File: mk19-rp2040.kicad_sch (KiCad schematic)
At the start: 145 parts, among them J1 USB_C_Receptacle_USB2.0, J10 Conn_01x02, J11 Conn_01x03_Socket, J12 USB_C_Receptacle_USB2.0, J13 USB_C_Receptacle_USB2.0, J2 Conn_01x03_Socket, J3 Conn_01x02_Socket, J4 Conn_01x06_Socket, J5 Conn_01x02, J6 Conn_01x02_Socket, J7 Conn_01x02_Socket, J8 Conn_01x02_Socket, J9 Conn_01x02_Socket, T1 Conn_01x01_Socket, T10 Conn_01x01_Socket, T11 Conn_01x01_Socket, T12 Conn_01x01_Socket, T13 Conn_01x01_Socket, T14 Conn_01x01_Socket, T15 Conn_01x01_Socket, T2 Conn_01x01_Socket, T3 Conn_01x01_Socket, T7 Conn_01x01_Socket, T9 Conn_01x01_Socket, U1 RP2040, U10 1N4148W_C81598, U11 1N4148W_C81598, U12 1N4148W_C81598, U13 1N4148W_C81598, U14 1N4148W_C81598, U15 1N4148W_C81598, U16 W25Q128JVSIQTR, U3 XC6210B332MR-G, U6 8_01A0_008200, U7 8_01A0_008200, U9 1N4148W_C81598, Y1 Crystal_GND24

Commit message: shipped to jlc
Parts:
- AUDIO1: footprint Connector_JST:JST_XH_B3B-XH-A_1x03_P2.50mm_Vertical -> Connector_JST:JST_XH_S3B-XH-A_1x03_P2.50mm_Horizontal
- J3: footprint Connector_JST:JST_XH_S2B-XH-A_1x02_P2.50mm_Horizontal -> Connector_JST:JST_XH_B2B-XH-A_1x02_P2.50mm_Vertical
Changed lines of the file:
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@@
 			)
 		)
-		(property "Footprint" "Connector_JST:JST_XH_S2B-XH-A_1x02_P2.50mm_Horizontal"
+		(property "Footprint" "Connector_JST:JST_XH_B2B-XH-A_1x02_P2.50mm_Vertical"
 			(at 118.11 331.47 0)
 			(effects
@@
 			)
 		)
-		(property "Footprint" "Connector_JST:JST_XH_B3B-XH-A_1x03_P2.50mm_Vertical"
+		(property "Footprint" "Connector_JST:JST_XH_S3B-XH-A_1x03_P2.50mm_Horizontal"
 			(at 278.13 360.68 0)
 			(effects

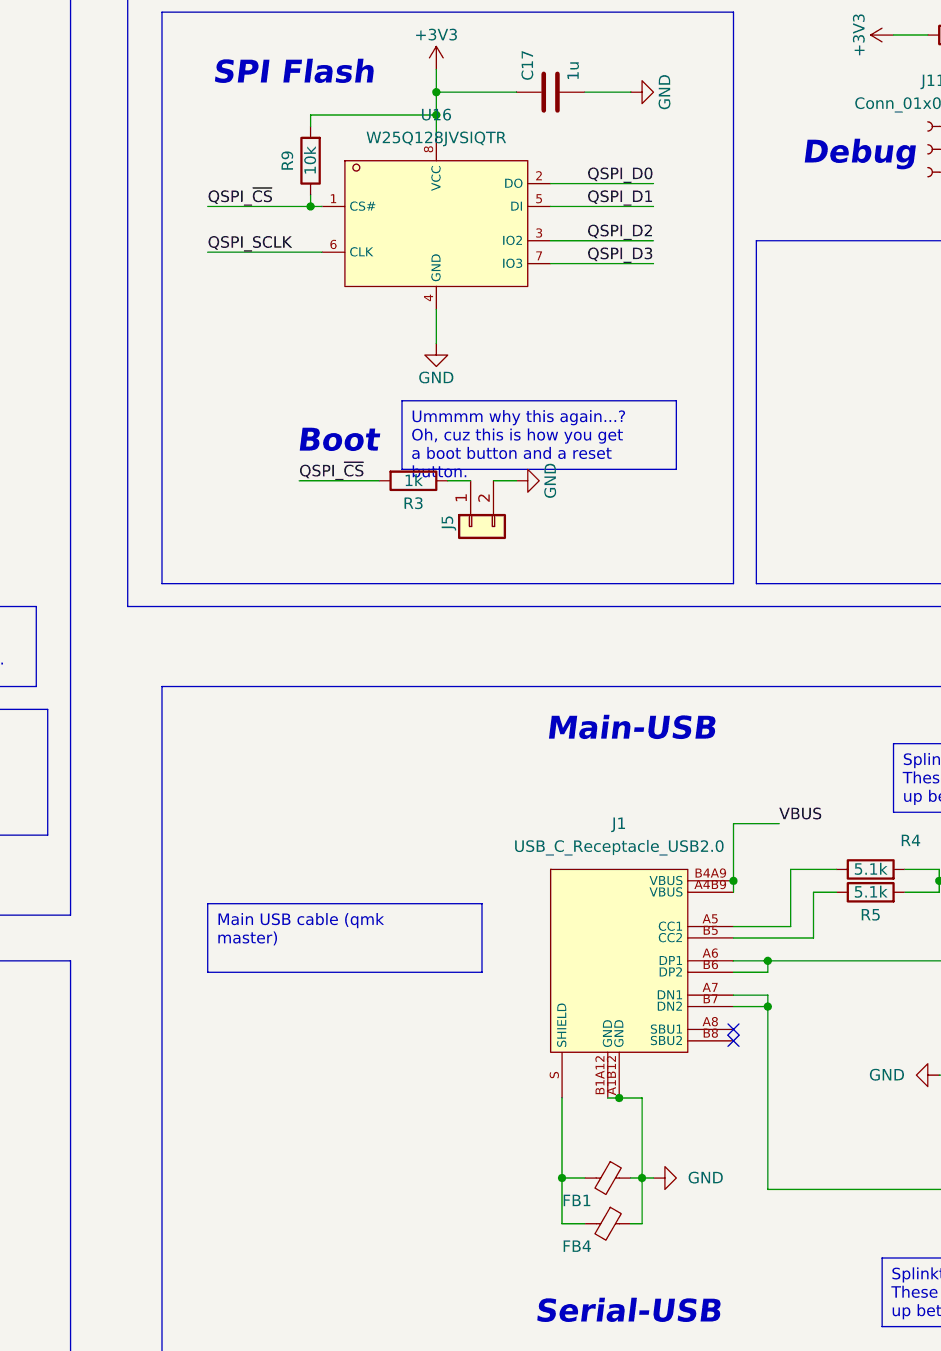
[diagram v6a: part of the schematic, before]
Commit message: fixing the manufacturing bugs - usb data crossed, flash pins 2 and 5 reversed, and v-cuts on wrong layer
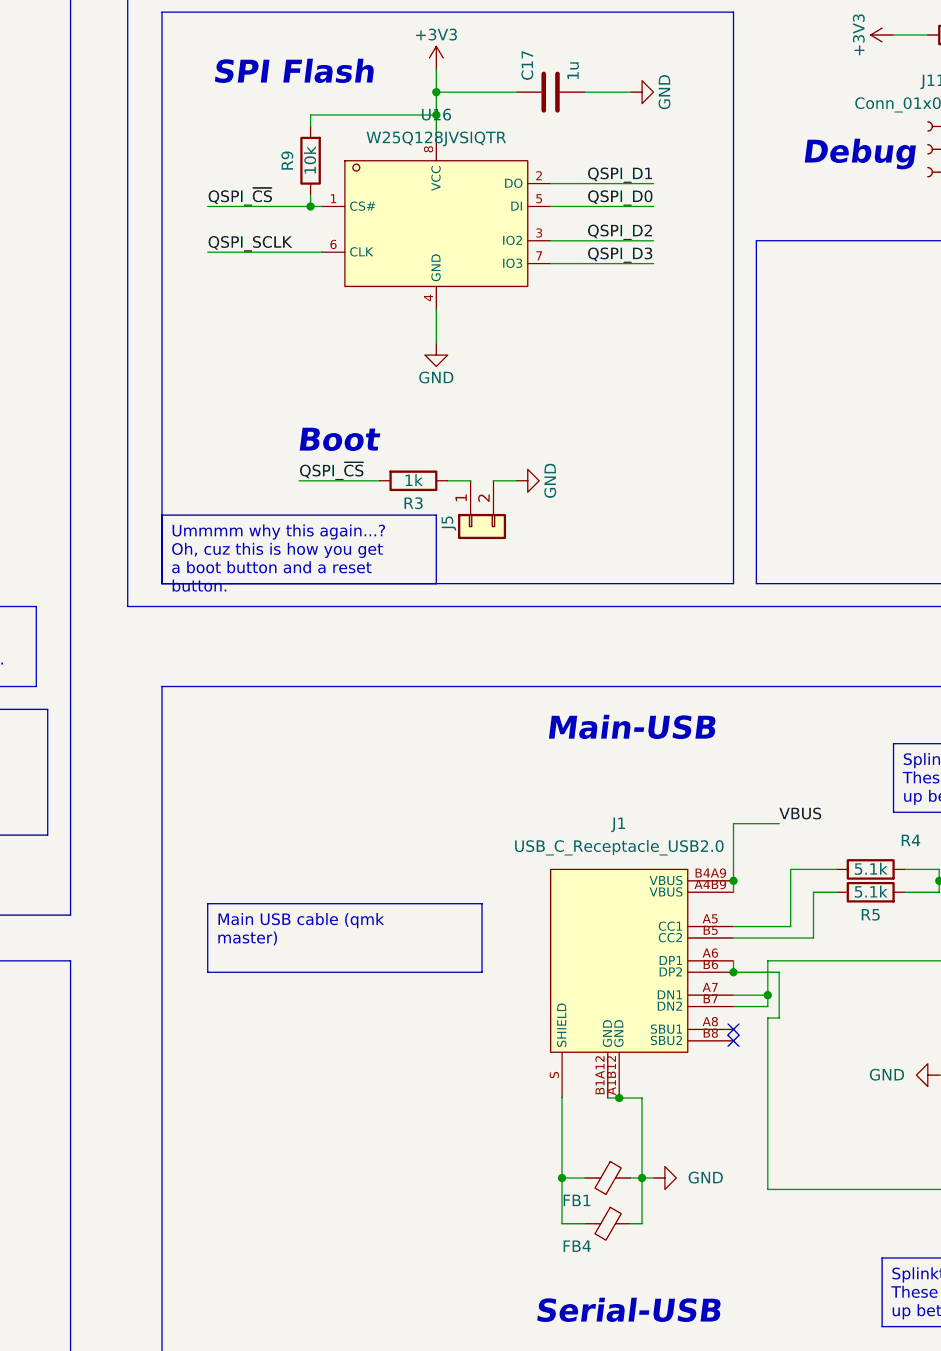
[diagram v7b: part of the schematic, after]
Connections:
- net QSPI_D0: now also U16.5 (DI); no longer U16.2 (DO)
- net QSPI_D1: now also U16.2 (DO); no longer U16.5 (DI)
- net USB-MAIN_+: now also J1.A6 (DP1), J1.B6 (DP2); no longer J1.A7 (DN1), J1.B7 (DN2)
- net USB-MAIN_-: now also J1.A7 (DN1), J1.B7 (DN2); no longer J1.A6 (DP1), J1.B6 (DP2)
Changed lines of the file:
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@@
 	)
 	(junction
-		(at 387.35 242.57)
-		(diameter 0)
-		(color 0 0 0 0)
-	)
-	(junction
 		(at 260.35 55.88)
 		(diameter 0)
@@
 	)
 	(junction
-		(at 525.78 255.27)
+		(at 387.35 241.3)
 		(diameter 0)
 		(color 0 0 0 0)
 	)
 	(junction
-		(at 161.29 166.37)
+		(at 525.78 255.27)
 		(diameter 0)
 		(color 0 0 0 0)
 	)
 	(junction
-		(at 222.25 166.37)
+		(at 161.29 166.37)
 		(diameter 0)
 		(color 0 0 0 0)
 	)
 	(junction
-		(at 189.23 54.61)
+		(at 222.25 166.37)
 		(diameter 0)
 		(color 0 0 0 0)
 	)
 	(junction
-		(at 387.35 237.49)
+		(at 189.23 54.61)
 		(diameter 0)
 		(color 0 0 0 0)
@@
 	)
 	(junction
+		(at 383.54 238.76)
+		(diameter 0)
+		(color 0 0 0 0)
+	)
+	(junction
 		(at 276.86 270.51)
 		(diameter 0)
@@
 	(wire
 		(pts
-			(xy 383.54 238.76) (xy 387.35 238.76)
-		)
-		(stroke
-			(width 0)
-			(type default)
-		)
-	)
-	(wire
-		(pts
 			(xy 198.12 83.82) (xy 198.12 90.17)
 		)
@@
 	(wire
 		(pts
-			(xy 383.54 241.3) (xy 387.35 241.3)
-		)
-		(stroke
-			(width 0)
-			(type default)
-		)
-	)
-	(wire
-		(pts
 			(xy 262.89 398.78) (xy 265.43 398.78)
 		)
@@
 	(wire
 		(pts
+			(xy 388.62 238.76) (xy 383.54 238.76)
+		)
+		(stroke
+			(width 0)
+			(type default)
+		)
+	)
+	(wire
+		(pts
 			(xy 384.81 293.37) (xy 393.7 293.37)
 		)
@@
 	(wire
 		(pts
+			(xy 388.62 243.84) (xy 388.62 238.76)
+		)
+		(stroke
+			(width 0)
+			(type default)
+		)
+	)
+	(wire
+		(pts
 			(xy 487.68 64.77) (xy 504.19 64.77)
 		)
@@
 	(wire
 		(pts
-			(xy 387.35 238.76) (xy 387.35 237.49)
-		)
-		(stroke
-			(width 0)
-			(type default)
-		)
-	)
-	(wire
-		(pts
 			(xy 480.06 46.99) (xy 480.06 44.45)
 		)
@@
 	(wire
 		(pts
-			(xy 383.54 237.49) (xy 387.35 237.49)
-		)
-		(stroke
-			(width 0)
-			(type default)
-		)
-	)
-	(wire
-		(pts
 			(xy 152.4 90.17) (xy 198.12 90.17)
 		)
@@
 	(wire
 		(pts
+			(xy 387.35 243.84) (xy 388.62 243.84)
+		)
+		(stroke
+			(width 0)
+			(type default)
+		)
+	)
+	(wire
+		(pts
 			(xy 561.34 52.07) (xy 563.88 52.07)
 		)
@@
 	(wire
 		(pts
-			(xy 387.35 242.57) (xy 387.35 262.89)
+			(xy 383.54 242.57) (xy 387.35 242.57)
 		)
 		(stroke
@@
 	(wire
 		(pts
-			(xy 387.35 241.3) (xy 387.35 242.57)
-		)
-		(stroke
-			(width 0)
-			(type default)
-		)
-	)
-	(wire
-		(pts
 			(xy 252.73 190.5) (xy 190.5 190.5)
 		)
@@
 	(wire
 		(pts
-			(xy 383.54 242.57) (xy 387.35 242.57)
+			(xy 350.52 140.97) (xy 359.41 140.97)
 		)
 		(stroke
@@
 	(wire
 		(pts
-			(xy 350.52 140.97) (xy 359.41 140.97)
+			(xy 525.78 64.77) (xy 528.32 64.77)
 		)
 		(stroke
@@
 	(wire
 		(pts
-			(xy 525.78 64.77) (xy 528.32 64.77)
+			(xy 274.32 284.48) (xy 276.86 284.48)
 		)
 		(stroke
@@
 	(wire
 		(pts
-			(xy 274.32 284.48) (xy 276.86 284.48)
+			(xy 223.52 397.51) (xy 223.52 401.32)
 		)
 		(stroke
@@
 	(wire
 		(pts
-			(xy 223.52 397.51) (xy 223.52 401.32)
+			(xy 387.35 262.89) (xy 387.35 243.84)
 		)
 		(stroke
@@
 	(wire
 		(pts
+			(xy 387.35 241.3) (xy 383.54 241.3)
+		)
+		(stroke
+			(width 0)
+			(type default)
+		)
+	)
+	(wire
+		(pts
 			(xy 212.09 132.08) (xy 212.09 148.59)
 		)
@@
 	(wire
 		(pts
+			(xy 387.35 242.57) (xy 387.35 241.3)
+		)
+		(stroke
+			(width 0)
+			(type default)
+		)
+	)
+	(wire
+		(pts
 			(xy 336.55 143.51) (xy 350.52 143.51)
 		)
@@
 	(wire
 		(pts
+			(xy 383.54 237.49) (xy 383.54 238.76)
+		)
+		(stroke
+			(width 0)
+			(type default)
+		)
+	)
+	(wire
+		(pts
 			(xy 76.2 118.11) (xy 80.01 118.11)
 		)
@@
 	(wire
 		(pts
+			(xy 387.35 237.49) (xy 387.35 241.3)
+		)
+		(stroke
+			(width 0)
+			(type default)
+		)
+	)
+	(wire
+		(pts
 			(xy 105.41 274.32) (xy 115.57 274.32)
 		)
@@
 	(text_box "Ummmm why this again...?\nOh, cuz this is how you get a boot button and a reset button."
 		(exclude_from_sim no)
-		(at 346.71 175.26 0)
+		(at 320.04 187.96 0)
 		(size 30.48 7.62)
 		(stroke
@@
 		)
 	)
-	(label "QSPI_D0"
+	(label "QSPI_D1"
 		(at 374.65 151.13 180)
 		(fields_autoplaced yes)
@@
 		)
 	)
-	(label "QSPI_D1"
+	(label "QSPI_D0"
 		(at 374.65 153.67 180)
 		(fields_autoplaced yes)

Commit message: starting rev4 pruning and converting
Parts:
- removed AUDIO1, J2: Conn_01x03_Socket, Connector_JST:JST_XH_S3B-XH-A_1x03_P2.50mm_Horizontal, symbol Connector:Conn_01x03_Socket
- removed C16: 1u, ct-kicad:C0402, symbol ct-kicad:CL31B105KBHNNNE
- removed COL1, COL2, ROW1, ROW2: Conn_01x08_Socket, Connector_JST:JST_XH_B8B-XH-A_1x08_P2.50mm_Vertical, symbol Connector:Conn_01x08_Socket
- removed CYBOARD-MACRO1: AFC04-S16ECA-00, ct-kicad:FPC-SMD_AFC04-S16ECA-00, symbol ct-kicad:AFC04-S16ECA-00
- removed D1: LED, LED_SMD:LED_0402_1005Metric, symbol Device:LED
- removed D3: B5817, Diode_SMD:D_SOD-323, symbol Device:D_Schottky
- removed D6: USBLC6-2P6_C2827693, ct-kicad:SOT-666-6_L1.6-W1.2-P0.50-LS1.6-BL, symbol ct-kicad:USBLC6-2P6_C2827693
- removed F2: Polyfuse, ct-kicad:F1206, symbol ct-kicad:RF1989-000
- removed FAL1, FAL2, PWM1, VANILED1: Conn_01x08_Socket, Connector_JST:JST_XH_S8B-XH-A_1x08_P2.50mm_Horizontal, symbol Connector:Conn_01x08_Socket
- removed FB1, FB2, FB3, FB4, FB5, FB6: FerriteBead_Small, Inductor_SMD:L_0603_1608Metric, symbol Device:FerriteBead_Small
- removed J13: USB_C_Receptacle_USB2.0, ct-kicad:USB-C-SMD_12P-P0.50-H-F_TYPE-C-31-M-14, symbol ct-kicad:TYPE-C-31-M-14
- removed JP1, JP4: SolderJumper_3_Open, Jumper:SolderJumper-3_P1.3mm_Open_Pad1.0x1.5mm, symbol Jumper:SolderJumper_3_Open
- removed JP5, JP6: SolderJumper_2_Open, Jumper:SolderJumper-2_P1.3mm_Open_RoundedPad1.0x1.5mm, symbol Jumper:SolderJumper_2_Open
- removed PWR-EXT-IN1: Conn_01x02_Socket, Connector_JST:JST_XH_S2B-XH-A_1x02_P2.50mm_Horizontal, symbol Connector:Conn_01x02_Socket
- removed PWR-OUT2: Conn_01x03_Socket, Connector_PinSocket_2.54mm:PinSocket_1x03_P2.54mm_Vertical, symbol Connector:Conn_01x03_Socket
- removed R1: 1k, ct-kicad:R0402, symbol Device:R
- removed R13, R14: 5.1k, ct-kicad:R0402, symbol ct-kicad:1206W4F1002T5E
- removed R21, R22: 5.1k, ct-kicad:R0402, symbol Device:R
- removed T10, T11, T12, T13, T14, T15, T9: Conn_01x01_Socket, TestPoint:TestPoint_Pad_1.0x1.0mm, symbol Connector:Conn_01x01_Socket
- removed T3, T7: Conn_01x01_Socket, Connector_Pin:Pin_D1.0mm_L10.0mm, symbol Connector:Conn_01x01_Socket
- removed U14, U15: 1N4148W_C81598, ct-kicad:SOD-123F_L2.7-W1.6-LS3.8-RD, symbol kicad-symbols:1N4148W_C81598
- removed U6, U7: 8_01A0_008200, ct-kicad:FPC-SMD_8P-P0.50_8.01A0.008200, symbol ct-kicad:8_01A0_008200
- added J13, J14, J15, J16, J2: ~, kicad-libraries:FFC-SMD_FFC05001-12SBA124W5M, symbol vik:vik-keyboard-connector
- J12: value USB_C_Receptacle_USB2.0 -> TRRS; symbol ct-kicad:TYPE-C-31-M-14 -> Connector_Audio:AudioJack4; now left out of the parts list
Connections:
- net +3V3: now also J13.1 (3V3), J14.1 (3V3), J15.1 (3V3), J16.1 (3V3), J2.1 (3V3)
- net +5V: now also J16.6 (5V)
- net GND: now also J12.T, J13.2 (GND), J14.2 (GND), J15.2 (GND), J16.2 (GND), J2.2 (GND); no longer J12.A1B12 (GND), J12.B1A12 (GND)
- net LCD1_CS: now also J16.10 (SPI_CS)
- net LCD_BL: now also J16.11 (MISO)
- net LCD_DC: now also J16.7 (GP_AD1)
- net LCD_RST: now also J16.9 (GP_AD2)
- net LED_MACRO_DI: no longer T2.1 (Pin_1)
- net PMW_CS: now also J13.10 (SPI_CS)
- net SPI1_CLK: now also J13.12 (SCLK), J16.12 (SCLK)
- net SPI1_MISO: now also J13.11 (MISO)
- net SPI1_MOSI: now also J13.8 (MOSI), J16.8 (MOSI)
- net Serial-RX: now also J12.R2; no longer J12.A6 (DP1), J12.B6 (DP2)
- net Serial-TX: now also J12.R1; no longer J12.A7 (DN1), J12.B7 (DN2)
- net Serial_VBUS: now also J12.S; no longer J12.A4B9 (VBUS), J12.B4A9 (VBUS)
- net AUDIO: no longer names the net of U1.2 (GPIO0)
- net LCD2_CS: no longer names the net of U1.29 (GPIO18)
- net VANILED_SIG1: no longer names the net of U1.34 (GPIO22)
- net VANILED_SIG2: no longer names the net of U1.35 (GPIO23)
- net VANILED_SIG3: no longer names the net of U1.36 (GPIO24)
- net VANILED_SIG4: no longer names the net of U1.37 (GPIO25)
- net fal1-r1 renamed encoder2-r1
- net encoder2-r1: now also J15.7 (GP_AD1)
- net fal1-r2 renamed encoder2-r2
- net encoder2-r2: now also J15.9 (GP_AD2)
- net fal2-r1 renamed encoder1-r1
- net encoder1-r1: now also J14.7 (GP_AD1)
- net fal2-r2 renamed encoder1-r2
- net encoder1-r2: now also J14.9 (GP_AD2)
- net rkjxt-a renamed encoder3-r2
- net encoder3-r2: now also J2.9 (GP_AD2)
- net rkjxt-b renamed encoder3-r1
- net encoder3-r1: now also J2.7 (GP_AD1)
- no-connect marks 14 -> 43
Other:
- note added: "Encoder1 (top, back)"
- note added: "Encoder2 (top, front)"
- note added: "Encoder3 (ring)"
- note added: "LCD"
- note removed: "5-way breakout"
- note removed: "Audio breakout"
- note removed: "Falcon1 connector"
- note removed: "Falcon2 connector"
- note removed: "GC9A01 LCDs"
- note removed: "Indicators From screen, to extra"
- note removed: "LED external power input"
- note removed: "Power LED"
- note removed: "RKJXT extender"
- note removed: "Row & Col breakouts"
- note removed: "Screen-USB"
- note removed: "Screen-USB ESD"
- note removed: "To Macropad Cyboard expander"
- note removed: "Vanity LED breakout"
- moved on the sheet: J4, J7, J8, J9, U10, U11, U12, U13, U9
